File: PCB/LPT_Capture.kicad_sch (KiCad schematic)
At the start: 12 parts, among them J1 USB3155-XX-X_REVA, J2 DB25 Male, U1 FT245RL

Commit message: caps units, sch clutter
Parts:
- C1, C3: value 0.1u -> 100n; footprint 000_LOCAL:C_0805_2012Metric -> 000_LOCAL:C_0805
- C2: footprint 000_LOCAL:C_0805_2012Metric -> 000_LOCAL:C_0805
- C4: value 0.01u -> 10n; footprint 000_LOCAL:C_0805_2012Metric -> 000_LOCAL:C_0805
- FB1: footprint 000_LOCAL:L_0805_2012Metric -> 000_LOCAL:L_0805
- R1: footprint 000_LOCAL:R_0805_2012Metric -> 000_LOCAL:R_0805
- U1: footprint 000_LOCAL:SSOP-28_5.3x10.2mm_P0.65mm -> 000_LOCAL:SSOP-28
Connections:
- net 3v3: now also C1.1; no longer C1.2
- net GND: now also C1.2; no longer C1.1, RA1.2 (R2.1), RA1.7 (R2.2)
- net RST_ERR renamed ~{RST_ERR}
- net Select: no longer names the net of J2.13
- net ~{AutoLineFeed}: no longer names the net of J2.14 (P14)
- net ~{Select-Printer}: no longer names the net of J2.17 (P17)
- no-connect marks 9 -> 11
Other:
- note added: "Computer sets low to request auto linefeed."
- note added: "ONLINE"
- note added: "PE"
- note added: "~{AUTOFD}"
- note added: "~{RESET}"
- note added: "~{SELIN}"
- note removed: "Computer sets low to req autofeed."
- note removed: "PaperEnd"
- note removed: "RESET"
- moved on the sheet: C1

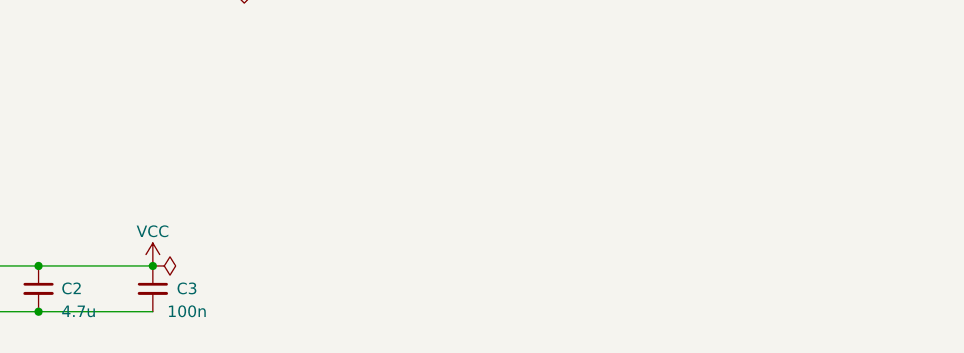
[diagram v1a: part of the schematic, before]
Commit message: add MPN to symbols, export fab_bom & centroid
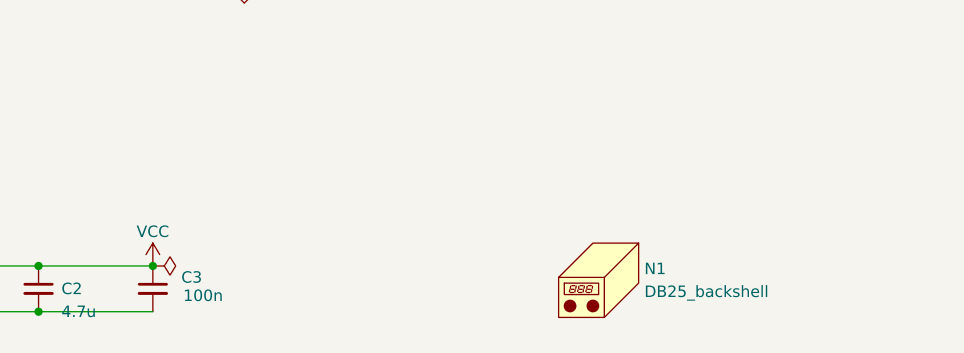
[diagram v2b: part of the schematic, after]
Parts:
- added N1: DB25_backshell, 000_LOCAL:db25_backshell, symbol 000_LOCAL:Housing
- C1, C3: MPN (none) -> 885012207045
- C2: MPN (none) -> GRM21BR71C475KE51L
- C4: MPN (none) -> 885012207039
- FB1: MPN (none) -> MH2029-400Y
- J1: MPN (none) -> USB3155-30-A
- J2: MPN (none) -> A-DS 25 LL/Z
- R1: MPN (none) -> RC0805JR-0747KL
- RA1, RA2, RA3: MPN (none) -> CAY16-101J4LF
- U1: MPN (none) -> FT245RL

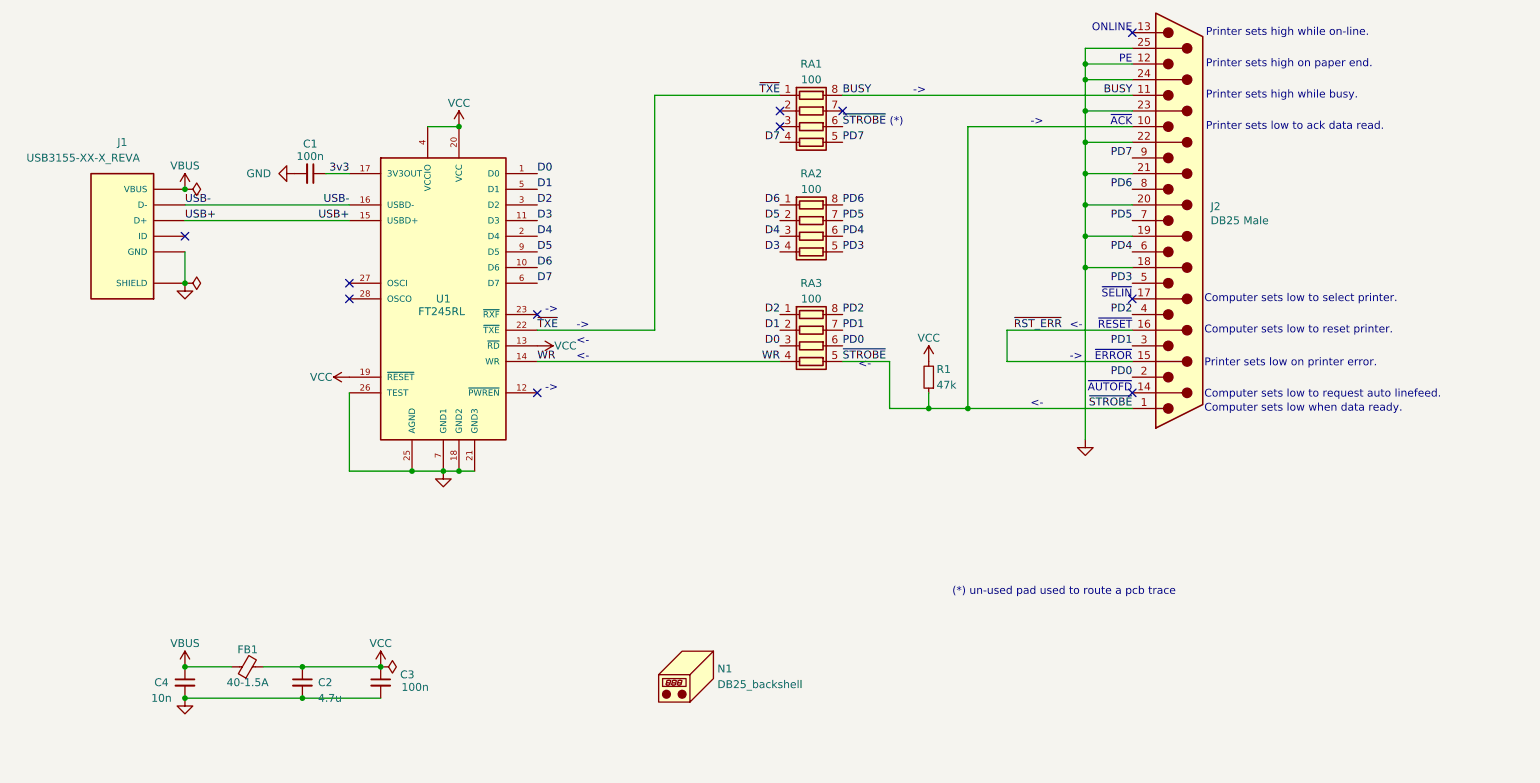
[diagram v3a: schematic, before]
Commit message: update eol FT245R to FT245RN
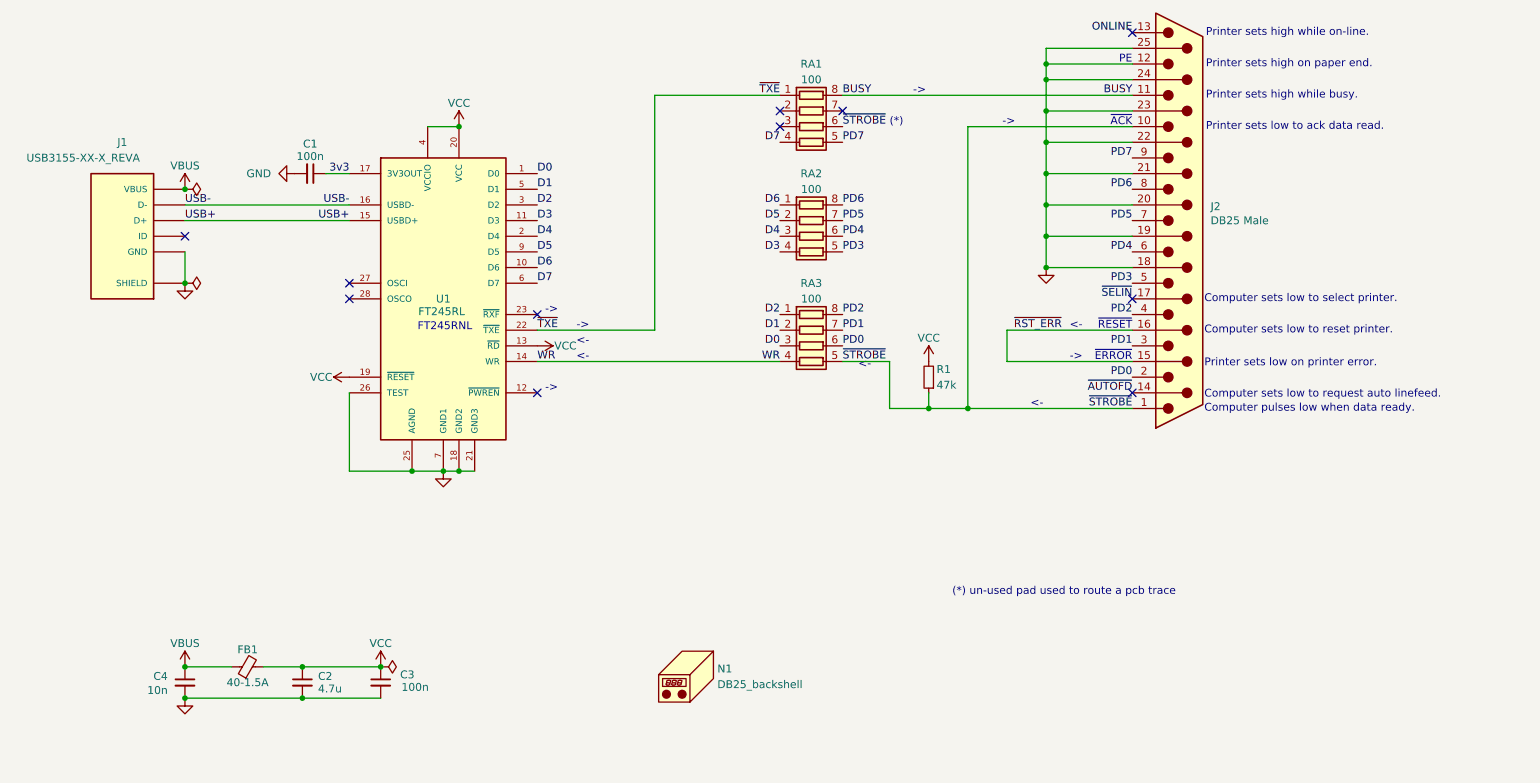
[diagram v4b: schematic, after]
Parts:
- U1: MPN FT245RL -> FT245RNL
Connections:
- net ONLINE: now reaches J2.13
- net ~{AUTOFD}: now reaches J2.14 (P14)
- net ~{SELIN}: now reaches J2.17 (P17)
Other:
- note added: "Computer pulses low when data ready."
- note added: "FT245RNL"
- note removed: "Computer sets low when data ready."
- note removed: "ONLINE"
- note removed: "~{AUTOFD}"
- note removed: "~{SELIN}"

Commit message: component library & models
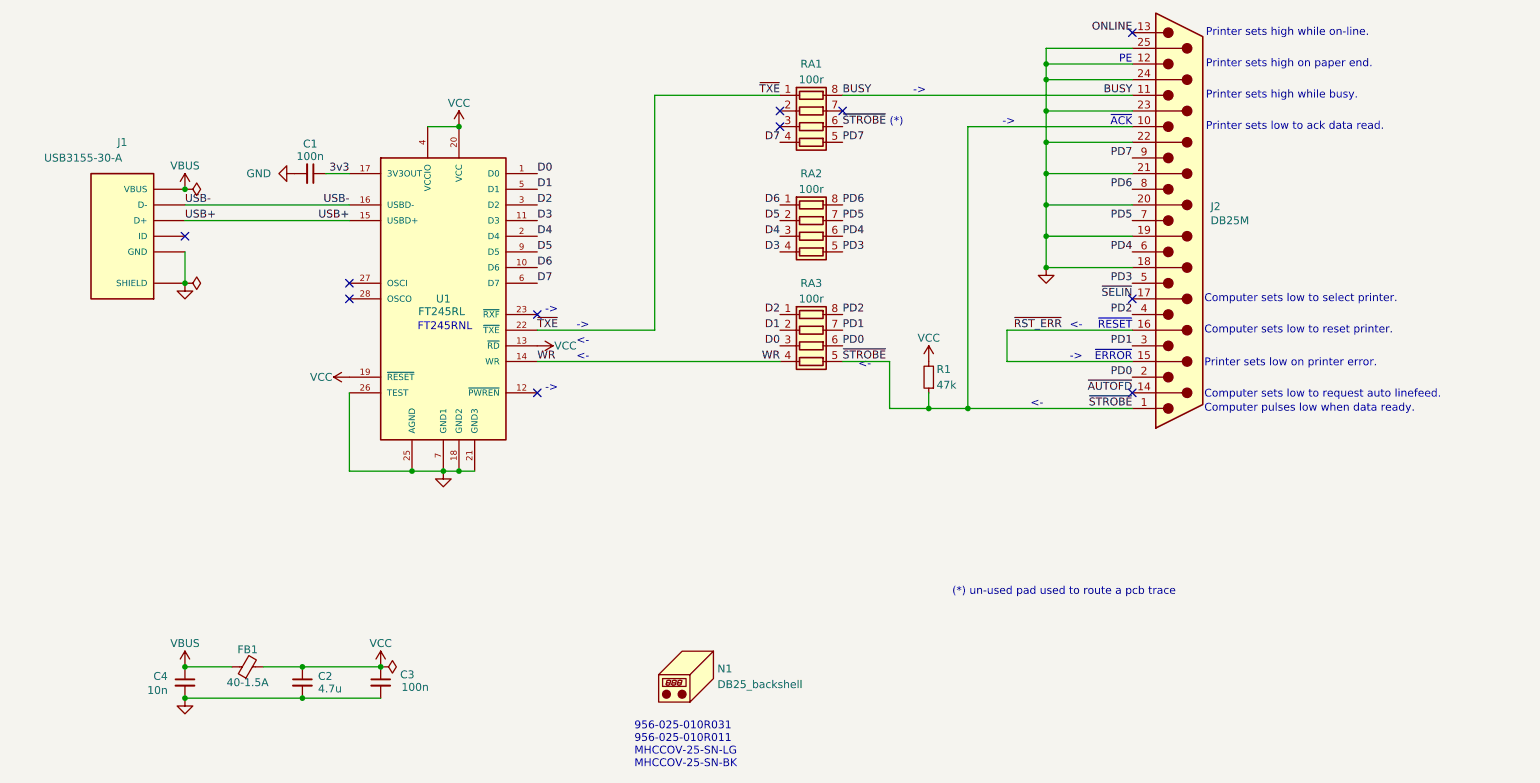
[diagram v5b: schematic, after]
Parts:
- J1: value USB3155-XX-X_REVA -> USB3155-30-A; footprint 000_LOCAL:GCT_USB3155-XX-X_REVA -> 000_LOCAL:GCT_USB3155-XX-X
- J2: value DB25 Male -> DB25M
- N1: footprint 000_LOCAL:db25_backshell -> 000_LOCAL:DSUB-25_Housing
- RA1, RA2, RA3: value 100 -> 100r
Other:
- note added: "956-025-010R031 956-025-010R011 MHCCOV-25-SN-LG MHCCOV-25-SN-BK"
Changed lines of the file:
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@@
+		)
+	)
+	(text "956-025-010R031\n956-025-010R011\nMHCCOV-25-SN-LG\nMHCCOV-25-SN-BK\n"
+		(exclude_from_sim no)
+		(at 130.048 172.72 0)
+		(effects
+			(font
+				(size 1.27 1.27)
+			)
+			(justify left top)
 		)
 	)
@@
 			)
 		)
-		(property "Value" "DB25 Male"
+		(property "Value" "DB25M"
 			(at 223.52 91.44 0)
 			(effects
@@
 			)
 		)
-		(property "Value" "100"
+		(property "Value" "100r"
 			(at 158.75 68.58 90)
 			(effects
@@
 			)
 		)
-		(property "Value" "USB3155-XX-X_REVA"
+		(property "Value" "USB3155-30-A"
 			(at 40.64 81.28 0)
 			(effects
@@
 			)
 		)
-		(property "Footprint" "000_LOCAL:GCT_USB3155-XX-X_REVA"
+		(property "Footprint" "000_LOCAL:GCT_USB3155-XX-X"
 			(at 46.99 93.98 0)
 			(effects
@@
 			)
 		)
-		(property "Value" "100"
+		(property "Value" "100r"
 			(at 158.75 104.14 90)
 			(effects
@@
 			)
 		)
-		(property "Footprint" "000_LOCAL:db25_backshell"
+		(property "Footprint" "000_LOCAL:DSUB-25_Housing"
 			(at 140.97 163.83 0)
 			(effects
@@
 			)
 		)
-		(property "Value" "100"
+		(property "Value" "100r"
 			(at 158.75 86.36 90)
 			(effects
